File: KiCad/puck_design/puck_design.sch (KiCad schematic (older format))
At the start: 18 parts, among them J1 Barrel_Jack, U1 ITG-3701, U2 BT840F, U3 TE832-M1, U4 MCP73831-2, U5 BQ297xy

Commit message: Added battery protection IC, resistors and MOS
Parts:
- added C6, C7: 4.7uF, symbol Device:C
- added C8: 0.1uF, symbol Device:C
- added Q1, Q2: CSD16406Q3, Package_TO_SOT_SMD:TDSON-8-1, symbol Transistor_FET:CSD16408Q5
- added R2, R3: 5M, symbol Device:R
- added R4: 2.2K, symbol Device:R
- added R5: 330, symbol Device:R
- added U?: VBAT, symbol puck_library:VBAT
- BH1: value Battery Holder -> BH
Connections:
- wire segments 84 -> 108
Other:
- moved on the sheet: BH1, C1, C2, C3, C4, C5, CX, R1, U1, U2, U3, U4

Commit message: Added footprint library
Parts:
- gave numbers to parts that had none: 3
- renumbered CX to CX1, CX to CX2, CX to CX3
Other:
- moved on the sheet: BH1, C1, C2, C3, C4, C5, C6, C7, C8, CX1, CX2, CX3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

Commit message: Rearranged battery protection circuitry and added missing components
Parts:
- removed J1: Barrel_Jack, symbol Connector:Barrel_Jack
- removed U5: BQ297xy, Package_SON:WSON-6_1.5x1.5mm_P0.5mm, symbol Battery_Management:BQ297xy
- removed U6, U7, U8: VBAT, symbol puck_library:VBAT
- added C9: 4.7uF, symbol Device:C
- added J1: Coax_Jack, symbol Connector:Conn_Coaxial_Power
- added L1: 10uH, symbol pspice:INDUCTOR
- added U5: BQ29700DSER, symbol puck_library:BQ29700DSER
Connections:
- net labels added: +BATT, -BATT
- wire segments 108 -> 132
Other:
- moved on the sheet: BH1, C1, C2, C3, C4, C5, C6, C7, CX1, CX2, CX3, R1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

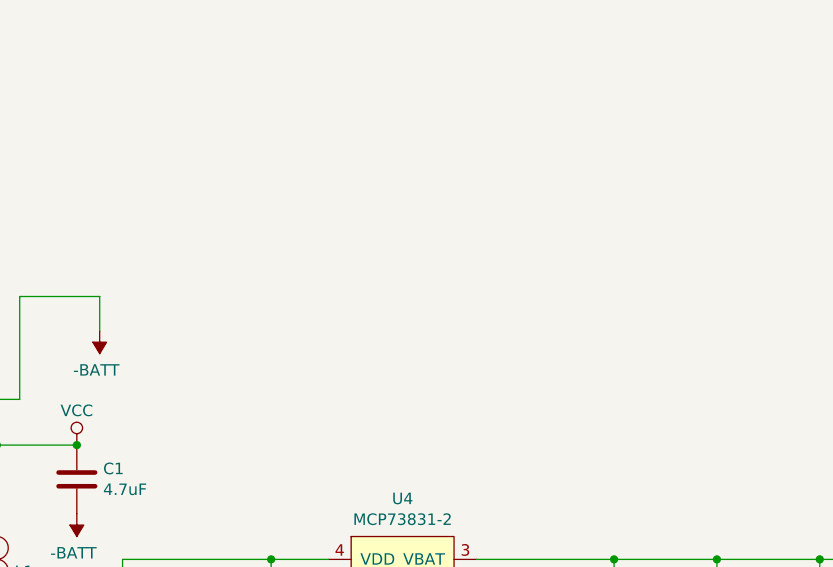
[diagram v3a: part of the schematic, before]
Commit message: Added footprints and associated to symbols
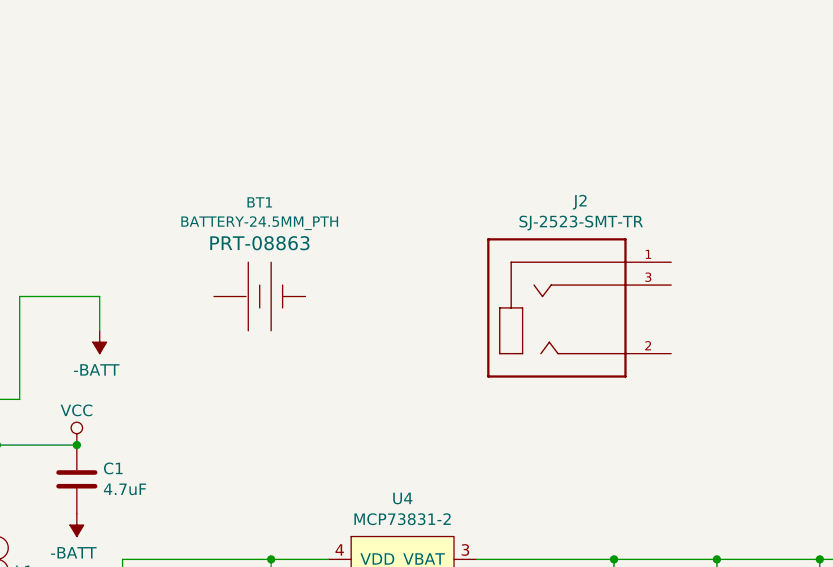
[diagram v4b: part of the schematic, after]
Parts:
- added BT1: BATTERY-24.5MM_PTH, puck_footprints:BATTCON_24.5MM_PTH, symbol puck_library:BATTERY-24.5MM_PTH
- added J2: SJ-2523-SMT-TR, puck_footprints:CUI_SJ-2523-SMT-TR, symbol puck_library:SJ-2523-SMT-TR
- BH1: footprint (none) -> puck_footprints:BATTCON_24.5MM_PTH
- C1, C2, C3, C4, C5, C6, C7, C8, C9, CX1, CX2, CX3: footprint (none) -> puck_footprints:CAPC2012X140N
- J1: footprint (none) -> puck_footprints:CUI_SJ-2523-SMT-TR
- Q1, Q2: footprint Package_TO_SOT_SMD:TDSON-8-1 -> puck_footprints:CSD16406Q3
- R1, R4, R5: footprint (none) -> puck_footprints:0805-NO
- R2, R3: footprint (none) -> puck_footprints:RESC1608X55
- U1: footprint (none) -> puck_footprints:ITG-3701
- U2: footprint XCVR_BT840F -> puck_footprints:BT840F
- U3: footprint (none) -> puck_footprints:832M1
- U4: footprint (none) -> puck_footprints:MCP73831T_2ATI_OT
- U5: footprint (none) -> puck_footprints:BQ29700DSER

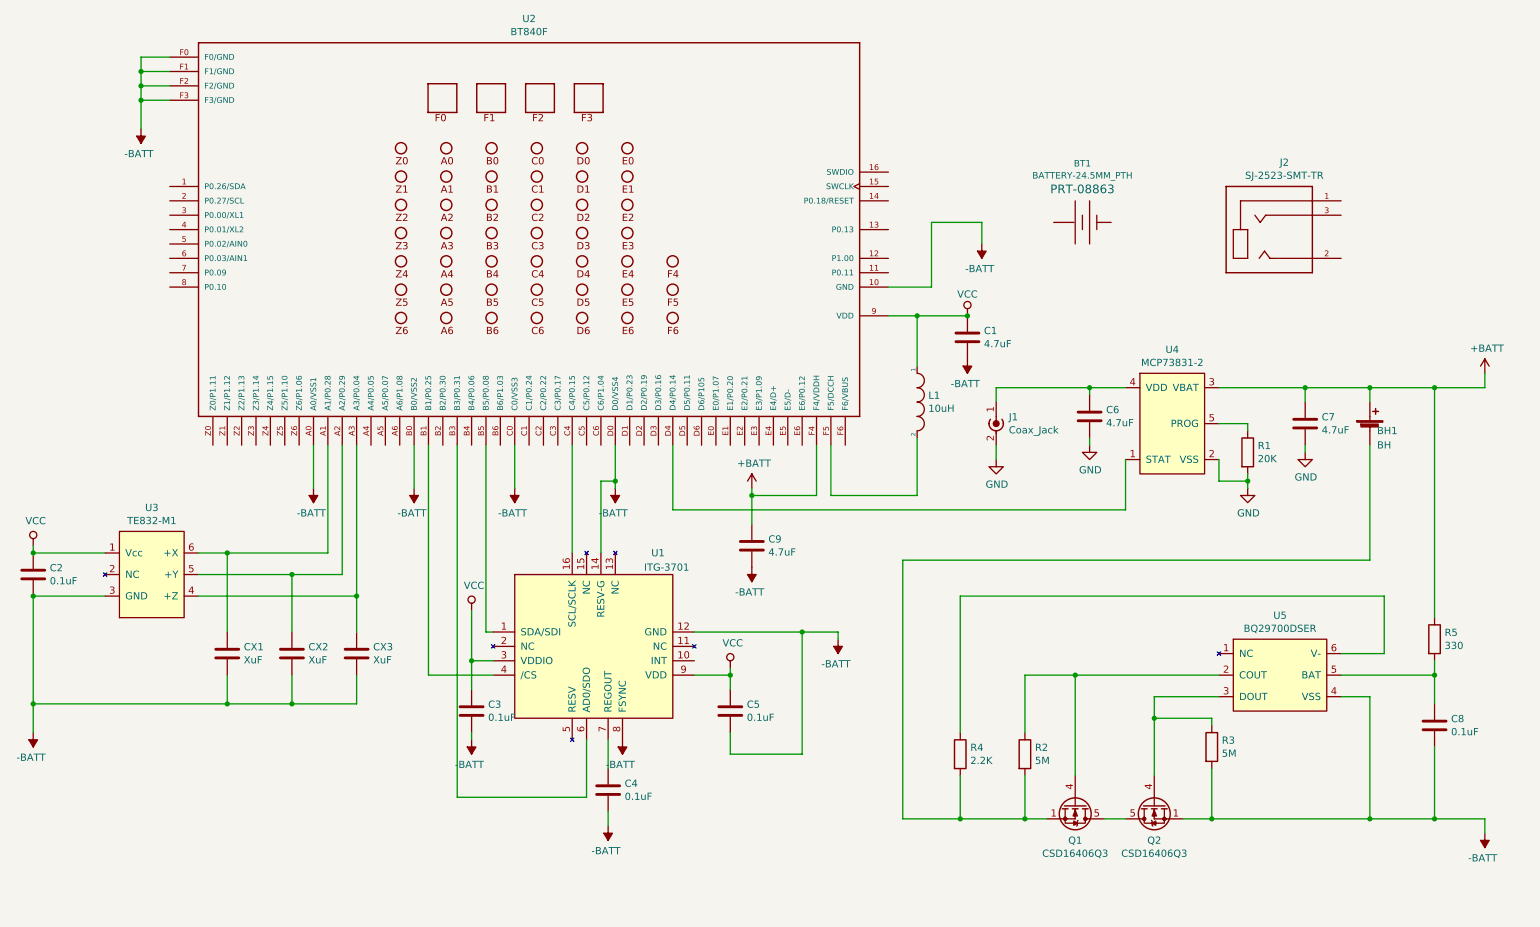
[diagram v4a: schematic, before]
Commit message: Changed pinout of accelerometer (X, Y) and charger IC status (to pin D6)
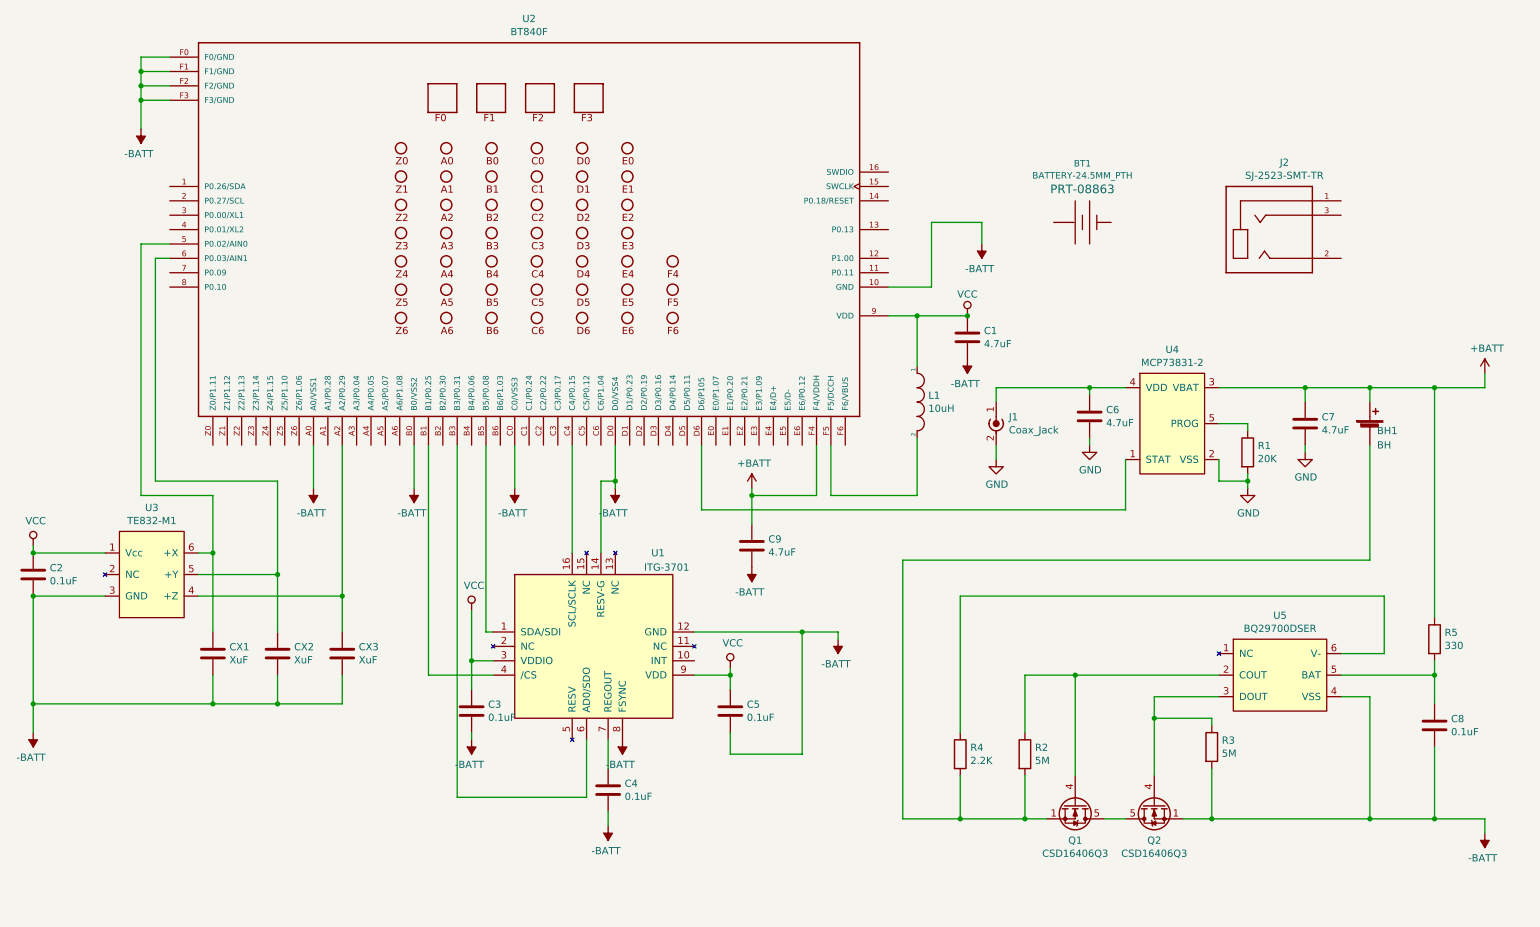
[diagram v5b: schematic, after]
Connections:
- net at CX3.1, U3.4 (+Z): now also U2.A2 (A2/P0.29); no longer U2.A3 (A3/P0.04)
- net at CX2.1, U3.5 (+Y): now also U2.6 (P0.03/AIN1); no longer U2.A2 (A2/P0.29)
- net at CX1.1, U3.6 (+X): now also U2.5 (P0.02/AIN0); no longer U2.A1 (A1/P0.28)
- net at U2.D4 (D4/P0.14): no longer U4.1 (STAT)
- net at U2.D6 (D6/P105): now also U4.1 (STAT)
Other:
- moved on the sheet: CX1, CX2, CX3
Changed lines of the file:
@@
 	1    0    0    -1
 $EndComp
-Wire Wire Line
-	2750 3550 2750 4300
-Wire Wire Line
-	2850 4450 2850 3550
-Wire Wire Line
-	2950 4600 2950 3550
 $Comp
 L power:VCC #PWR0104
@@
 L Device:C CX3
 U 1 1 5C143212
-P 2950 5000
-F 0 "CX3" H 3065 5046 50  0000 L CNN
-F 1 "XuF" H 3065 4955 50  0000 L CNN
-F 2 "puck_footprints:CAPC2012X140N" H 2988 4850 50  0001 C CNN
-F 3 "~" H 2950 5000 50  0001 C CNN
-	1    2950 5000
+P 2850 5000
+F 0 "CX3" H 2965 5046 50  0000 L CNN
+F 1 "XuF" H 2965 4955 50  0000 L CNN
+F 2 "puck_footprints:CAPC2012X140N" H 2888 4850 50  0001 C CNN
+F 3 "~" H 2850 5000 50  0001 C CNN
+	1    2850 5000
 	1    0    0    -1
 $EndComp
@@
 L Device:C CX2
 U 1 1 5C145DBB
-P 2500 5000
-F 0 "CX2" H 2615 5046 50  0000 L CNN
-F 1 "XuF" H 2615 4955 50  0000 L CNN
-F 2 "puck_footprints:CAPC2012X140N" H 2538 4850 50  0001 C CNN
-F 3 "~" H 2500 5000 50  0001 C CNN
-	1    2500 5000
+P 2400 5000
+F 0 "CX2" H 2515 5046 50  0000 L CNN
+F 1 "XuF" H 2515 4955 50  0000 L CNN
+F 2 "puck_footprints:CAPC2012X140N" H 2438 4850 50  0001 C CNN
+F 3 "~" H 2400 5000 50  0001 C CNN
+	1    2400 5000
 	1    0    0    -1
 $EndComp
@@
 L Device:C CX1
 U 1 1 5C146CAE
-P 2050 5000
-F 0 "CX1" H 2165 5046 50  0000 L CNN
-F 1 "XuF" H 2165 4955 50  0000 L CNN
-F 2 "puck_footprints:CAPC2012X140N" H 2088 4850 50  0001 C CNN
-F 3 "~" H 2050 5000 50  0001 C CNN
-	1    2050 5000
-	1    0    0    -1
-$EndComp
-Wire Wire Line
-	2050 5350 2500 5350
-Wire Wire Line
-	2500 5150 2500 5350
-Connection ~ 2500 5350
-Wire Wire Line
-	2500 5350 2950 5350
-Wire Wire Line
-	2750 4300 2050 4300
-Wire Wire Line
-	1850 4600 2950 4600
-Wire Wire Line
-	2950 5350 2950 5150
-Wire Wire Line
-	2050 5350 2050 5150
+P 1950 5000
+F 0 "CX1" H 2065 5046 50  0000 L CNN
+F 1 "XuF" H 2065 4955 50  0000 L CNN
+F 2 "puck_footprints:CAPC2012X140N" H 1988 4850 50  0001 C CNN
+F 3 "~" H 1950 5000 50  0001 C CNN
+	1    1950 5000
+	1    0    0    -1
+$EndComp
 Connection ~ 700  4600
 Wire Wire Line
 	700  4600 1200 4600
-Connection ~ 2050 5350
-Wire Wire Line
-	1850 4450 2500 4450
+Wire Wire Line
+	1850 4450 2400 4450
 Wire Wire Line
 	700  4600 700  5350
-Wire Wire Line
-	700  5350 2050 5350
 Connection ~ 700  5350
 Wire Wire Line
 	700  5350 700  5550
-Wire Wire Line
-	2050 4850 2050 4300
-Connection ~ 2050 4300
-Wire Wire Line
-	2050 4300 1850 4300
-Wire Wire Line
-	2500 4850 2500 4450
-Connection ~ 2500 4450
-Wire Wire Line
-	2500 4450 2850 4450
-Wire Wire Line
-	2950 4850 2950 4600
-Connection ~ 2950 4600
 $Comp
 L puck_library:MCP73831-2 U4
@@
 	1    0    0    -1
 $EndComp
-Wire Wire Line
-	5150 3550 5150 4000
 Wire Wire Line
 	8300 3650 8300 4000
@@
 	0    1    1    0
 $EndComp
-Wire Wire Line
-	5150 4000 8300 4000
 Wire Wire Line
 	6650 2450 6950 2450
@@
 	1    0    0    -1
 $EndComp
+Wire Wire Line
+	1650 2150 1450 2150
+Wire Wire Line
+	1450 2150 1450 3900
+Wire Wire Line
+	1450 3900 1950 3900
+Wire Wire Line
+	1650 2250 1550 2250
+Wire Wire Line
+	1550 2250 1550 3800
+Wire Wire Line
+	1850 4600 2850 4600
+Wire Wire Line
+	2850 3550 2850 4600
+Wire Wire Line
+	2850 4600 2850 4850
+Connection ~ 2850 4600
+Wire Wire Line
+	2850 5350 2850 5150
+Wire Wire Line
+	1950 4850 1950 4300
+Connection ~ 1950 4300
+Wire Wire Line
+	1950 4300 1850 4300
+Wire Wire Line
+	1950 3900 1950 4300
+Wire Wire Line
+	700  5350 1950 5350
+Wire Wire Line
+	1950 5150 1950 5350
+Connection ~ 1950 5350
+Wire Wire Line
+	1950 5350 2400 5350
+Wire Wire Line
+	2400 5150 2400 5350
+Connection ~ 2400 5350
+Wire Wire Line
+	2400 5350 2850 5350
+Wire Wire Line
+	2400 4850 2400 4450
+Wire Wire Line
+	2400 3800 2400 4450
+Connection ~ 2400 4450
+Wire Wire Line
+	1550 3800 2400 3800
+Wire Wire Line
+	5350 3550 5350 4000
+Wire Wire Line
+	5350 4000 8300 4000
 $EndSCHEMATC
